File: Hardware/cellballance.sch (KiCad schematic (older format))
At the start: 54 parts

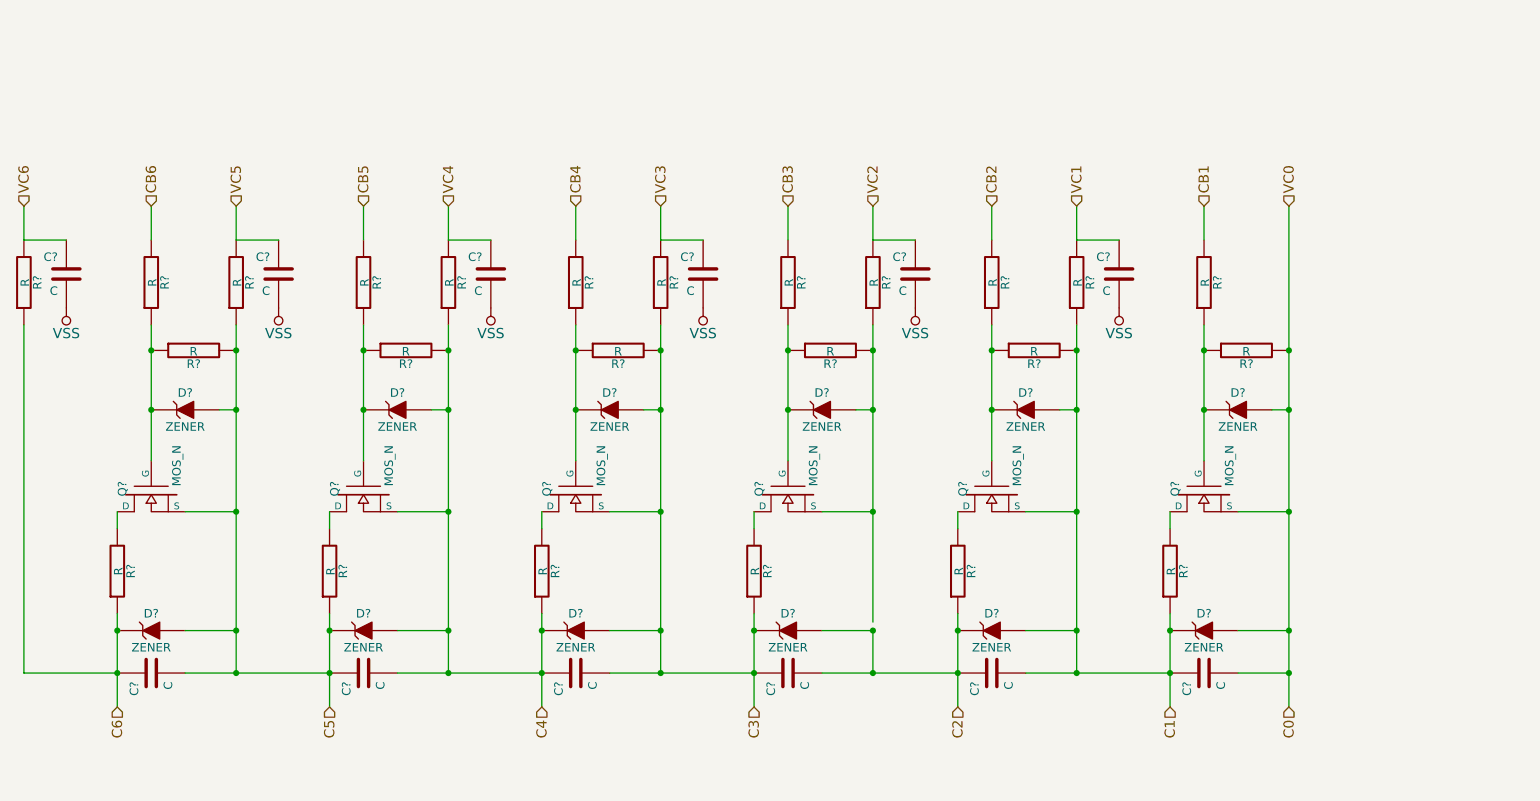
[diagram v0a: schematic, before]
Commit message: version 1 board completed
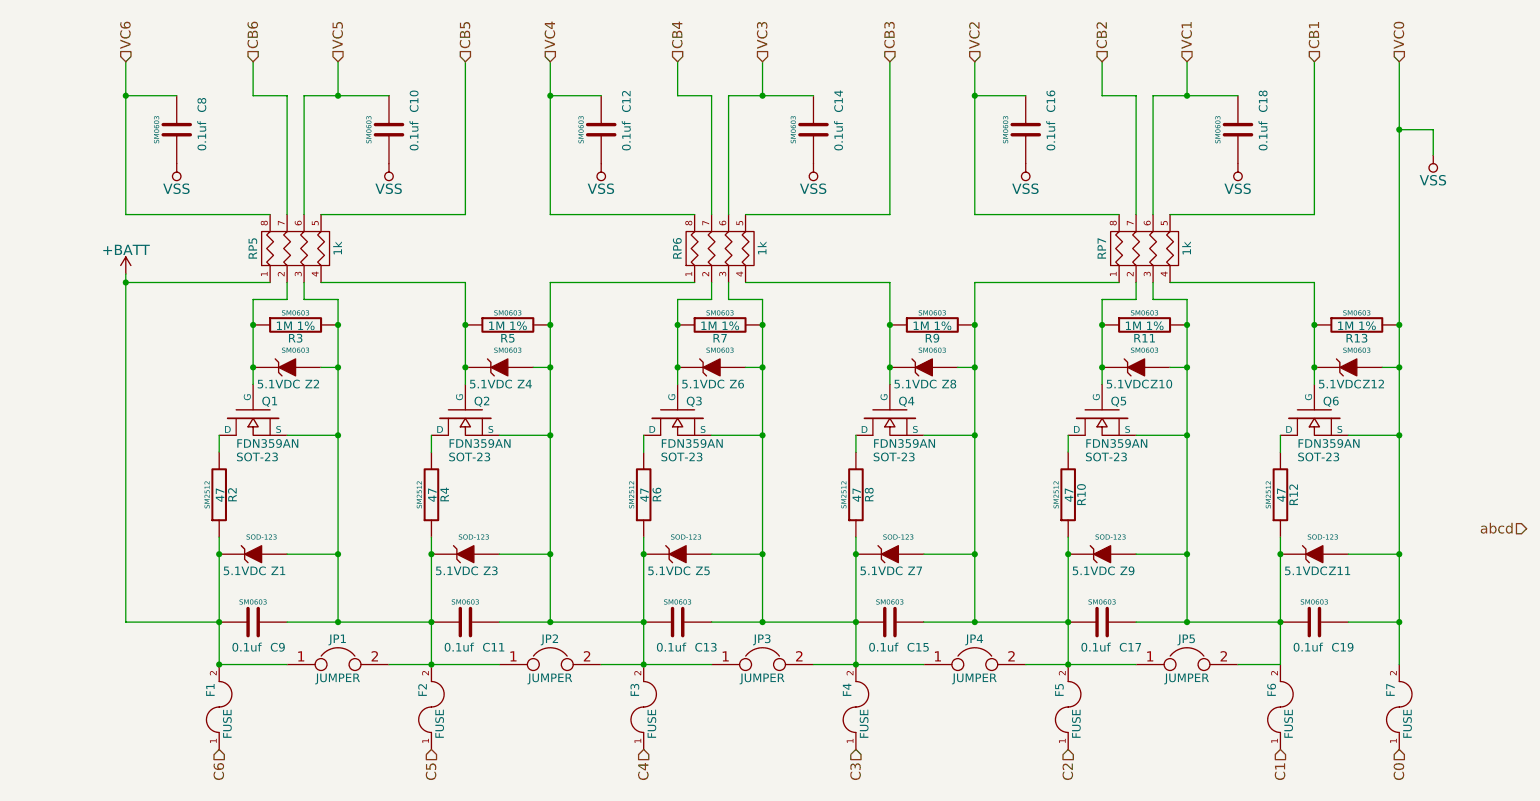
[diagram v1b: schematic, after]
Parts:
- removed C? (x11): C, symbol C
- removed D? (x12): ZENER, symbol ZENER
- removed Q? (x5): MOS_N, symbol MOS_N
- removed R? (x24): R, symbol R
- added C10, C11, C12, C13, C14, C15, C16, C17, C18, C8, C9: 0.1uf, SM0603, symbol C
- added F1, F2, F3, F4, F5, F6, F7: FUSE, symbol FUSE
- added JP1, JP2, JP3, JP4, JP5: JUMPER, symbol JUMPER
- added Q1, Q2, Q3, Q4, Q5: FDN359AN, SOT-23, symbol MOS_N
- added R10, R12, R2, R4, R6, R8: 47, SM2512, symbol R
- added R11, R13, R3, R5, R7, R9: 1M 1%, SM0603, symbol R
- added RP5, RP6, RP7: 1k, symbol R_PACK4
- added Z1, Z11, Z3, Z5, Z7, Z9: ZENER, SOD-123, symbol ZENER
- added Z10, Z12, Z2, Z4, Z6, Z8: ZENER, SM0603, symbol ZENER
- C19: renamed from C?; value C -> 0.1uf; footprint (none) -> SM0603; Rating (none) -> 50V
- Q6: renamed from Q?; value MOS_N -> FDN359AN; footprint (none) -> SOT-23
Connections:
- net C0: now also F7.1; no longer C19.2, Q6.S
- net C1: now also F6.1; no longer C19.1
- net C2: now also F5.1
- net C3: now also F4.1
- net C4: now also F3.1
- net C5: now also F2.1
- net C6: now also F1.1
- net CB1: now also RP7.5 (R4)
- net CB2: now also RP7.7 (R2)
- net CB3: now also RP6.5 (R4)
- net CB4: now also RP6.7 (R2)
- net CB5: now also RP5.5 (R4)
- net CB6: now also RP5.7 (R2)
- net VC1: now also C18.2, RP7.6 (R3)
- net VC2: now also C16.2, RP7.8 (R1)
- net VC3: now also C14.2, RP6.6 (R3)
- net VC4: now also C12.2, RP6.8 (R1)
- net VC5: now also C10.2, RP5.6 (R3)
- net VC6: now also C8.2, RP5.8 (R1)
- net VSS: now also C19.2, Q6.S, C10.1, C12.1, C14.1, C16.1, C18.1, C8.1, F7.2, R13.2, Z11.1 (A), Z12.1 (A)
- net at Q6.D: now also R12.2
- net at Q6.G: now also R13.1, RP7.4 (P4), Z12.2 (K)
- new net: C17.2, C19.1, F6.2, JP5.2, Q5.S, R11.2, R12.1, RP7.3 (P3), Z10.1 (A), Z11.2 (K), Z9.1 (A)
- new net: C15.2, C17.1, F5.2, JP4.2, JP5.1, Q4.S, R10.1, R9.2, RP7.1 (P1), Z7.1 (A), Z8.1 (A), Z9.2 (K)
- new net: Q5.D, R10.2
- new net: Q5.G, R11.1, RP7.2 (P2), Z10.2 (K)
- new net: Q4.D, R8.2
- new net: Q4.G, R9.1, RP6.4 (P4), Z8.2 (K)
- new net: C13.2, C15.1, F4.2, JP3.2, JP4.1, Q3.S, R7.2, R8.1, RP6.3 (P3), Z5.1 (A), Z6.1 (A), Z7.2 (K)
- new net: Q3.D, R6.2
- new net: Q3.G, R7.1, RP6.2 (P2), Z6.2 (K)
- new net: C11.2, C13.1, F3.2, JP2.2, JP3.1, Q2.S, R5.2, R6.1, RP6.1 (P1), Z3.1 (A), Z4.1 (A), Z5.2 (K)
- new net: Q2.D, R4.2
- new net: Q2.G, R5.1, RP5.4 (P4), Z4.2 (K)
- new net: C11.1, C9.2, F2.2, JP1.2, JP2.1, Q1.S, R3.2, R4.1, RP5.3 (P3), Z1.1 (A), Z2.1 (A), Z3.2 (K)
- new net: Q1.G, R3.1, RP5.2 (P2), Z2.2 (K)
- new net: Q1.D, R2.2
- new net +BATT: C9.1, F1.2, JP1.1, R2.1, RP5.1 (P1), Z1.2 (K)
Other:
- moved on the sheet: C19, Q6
